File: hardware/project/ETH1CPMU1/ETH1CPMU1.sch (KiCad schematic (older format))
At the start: 0 parts

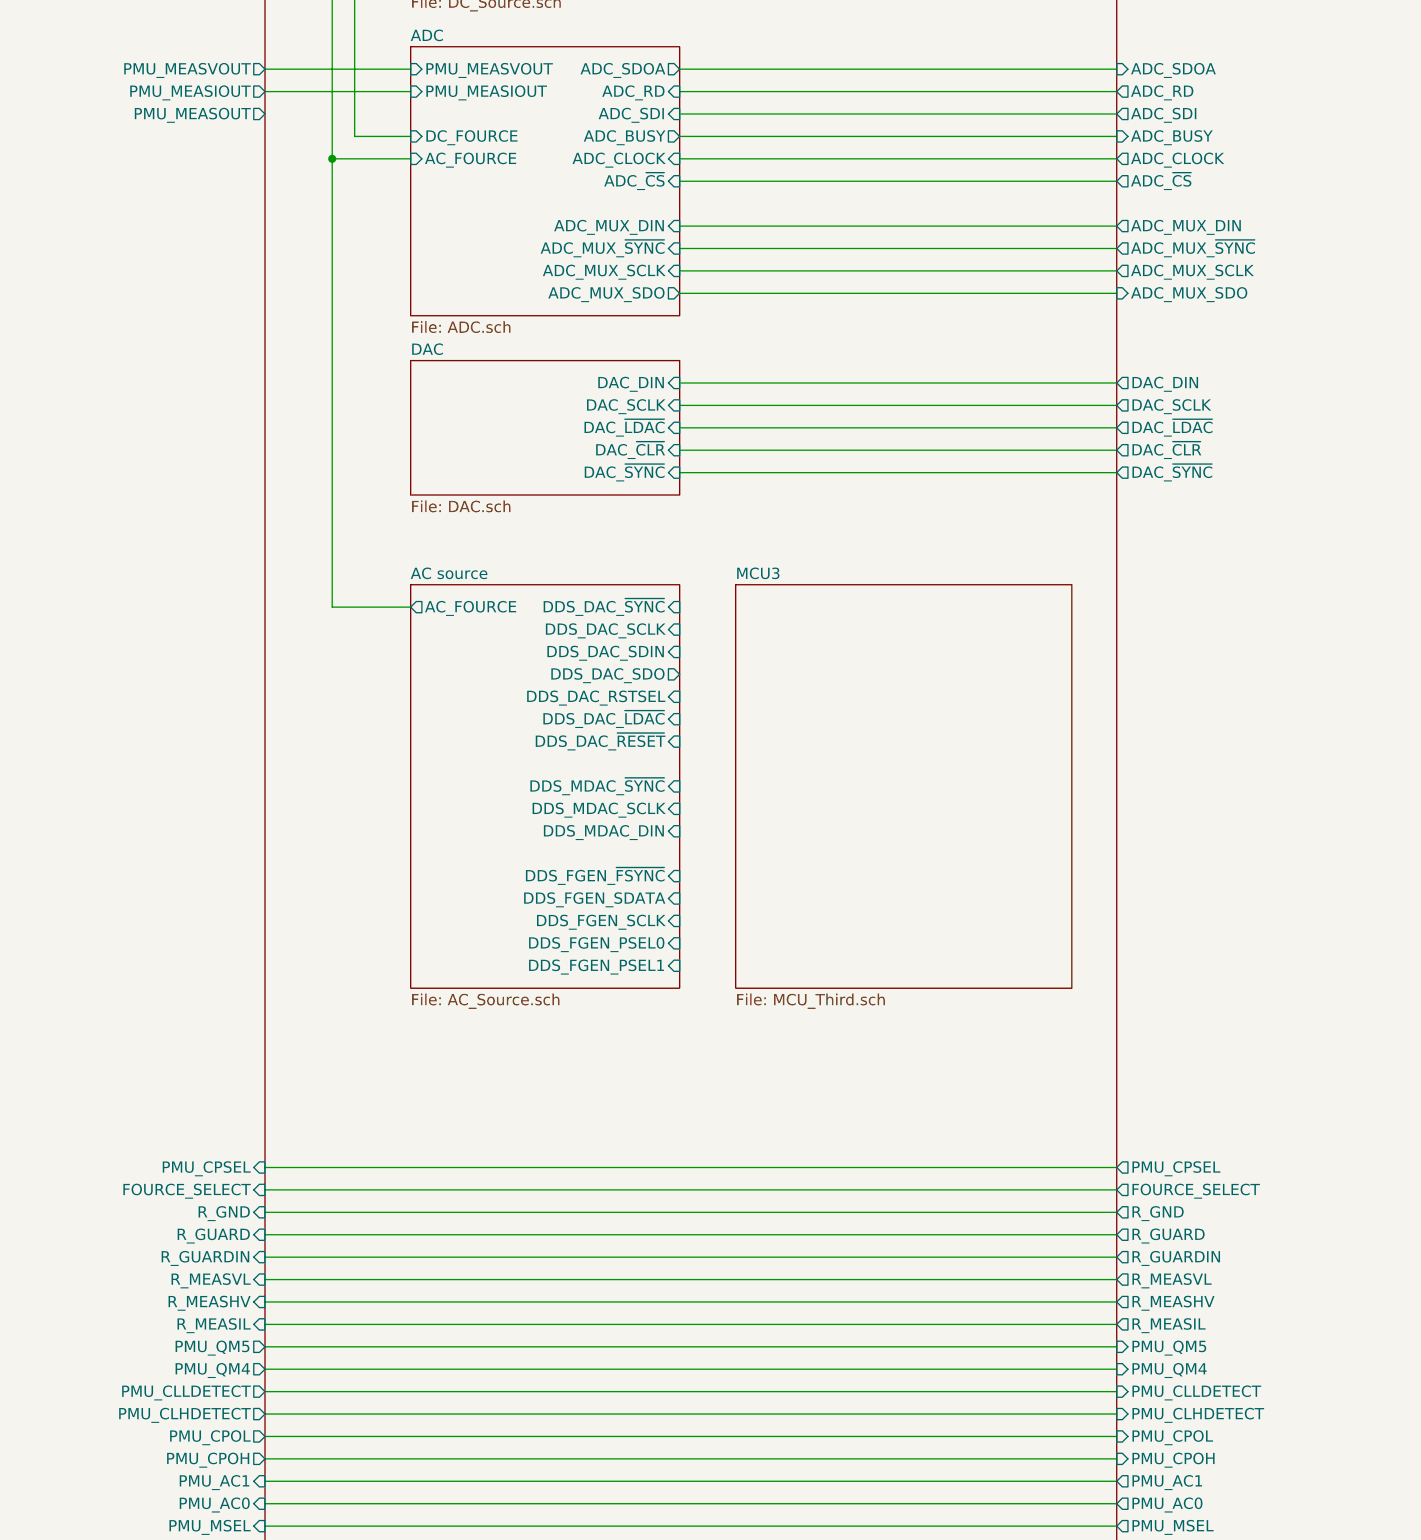
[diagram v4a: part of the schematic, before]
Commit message: New footprint development, changes in schematics.
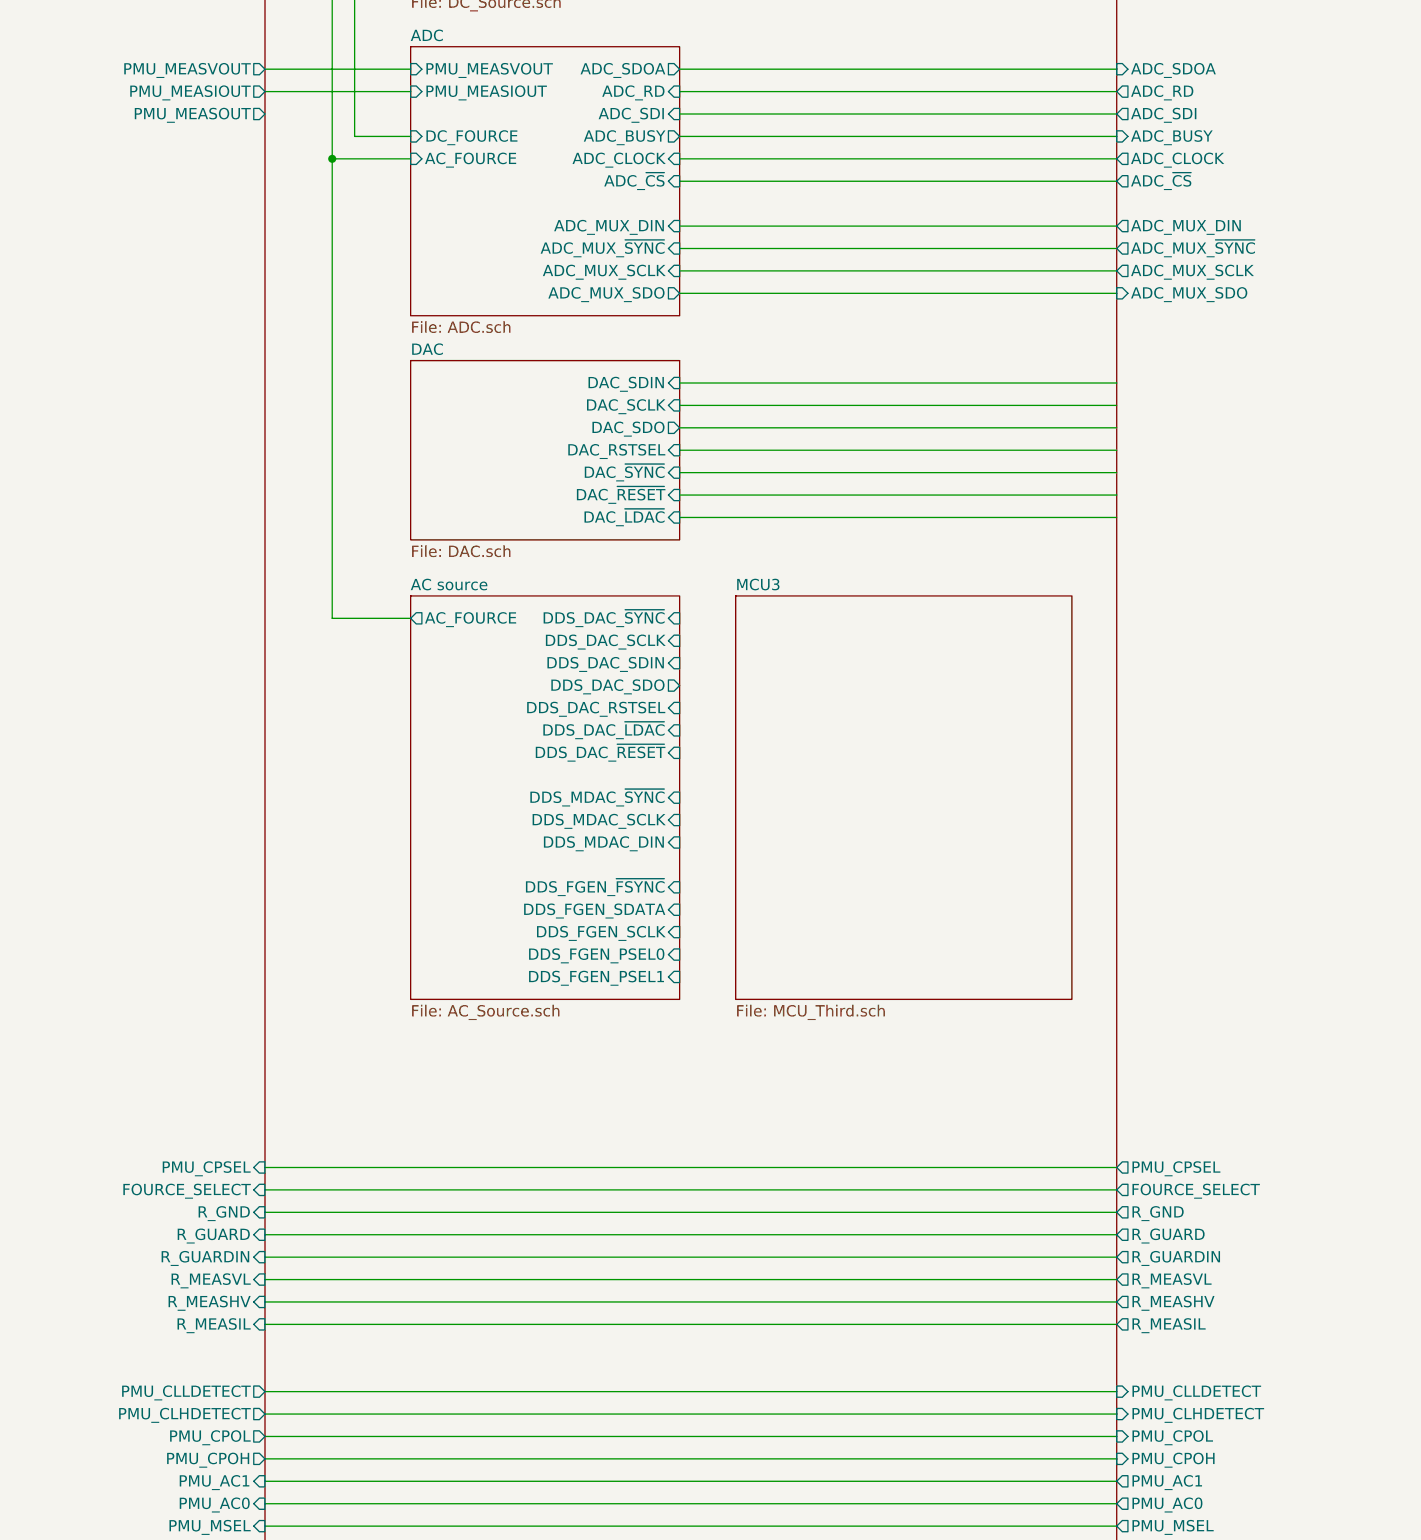
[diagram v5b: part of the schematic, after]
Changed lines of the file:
@@
 $EndSheet
 $Sheet
-S 3750 5200 1200 1800
+S 3750 5250 1200 1800
 U 5DF36C25
 F0 "AC source" 50
 F1 "AC_Source.sch" 50
-F2 "AC_FOURCE" O L 3750 5300 50
-F3 "DDS_DAC_~SYNC" I R 4950 5300 50
-F4 "DDS_DAC_SCLK" I R 4950 5400 50
-F5 "DDS_DAC_SDIN" I R 4950 5500 50
-F6 "DDS_MDAC_~SYNC" I R 4950 6100 50
-F7 "DDS_MDAC_SCLK" I R 4950 6200 50
-F8 "DDS_MDAC_DIN" I R 4950 6300 50
-F9 "DDS_DAC_SDO" O R 4950 5600 50
-F10 "DDS_DAC_~RESET" I R 4950 5900 50
-F11 "DDS_DAC_~LDAC" I R 4950 5800 50
-F12 "DDS_DAC_RSTSEL" I R 4950 5700 50
-F13 "DDS_FGEN_~FSYNC" I R 4950 6500 50
-F14 "DDS_FGEN_SDATA" I R 4950 6600 50
-F15 "DDS_FGEN_SCLK" I R 4950 6700 50
-F16 "DDS_FGEN_PSEL0" I R 4950 6800 50
-F17 "DDS_FGEN_PSEL1" I R 4950 6900 50
-$EndSheet
-$Sheet
-S 3750 4200 1200 600
+F2 "AC_FOURCE" O L 3750 5350 50
+F3 "DDS_DAC_~SYNC" I R 4950 5350 50
+F4 "DDS_DAC_SCLK" I R 4950 5450 50
+F5 "DDS_DAC_SDIN" I R 4950 5550 50
+F6 "DDS_MDAC_~SYNC" I R 4950 6150 50
+F7 "DDS_MDAC_SCLK" I R 4950 6250 50
+F8 "DDS_MDAC_DIN" I R 4950 6350 50
+F9 "DDS_DAC_SDO" O R 4950 5650 50
+F10 "DDS_DAC_~RESET" I R 4950 5950 50
+F11 "DDS_DAC_~LDAC" I R 4950 5850 50
+F12 "DDS_DAC_RSTSEL" I R 4950 5750 50
+F13 "DDS_FGEN_~FSYNC" I R 4950 6550 50
+F14 "DDS_FGEN_SDATA" I R 4950 6650 50
+F15 "DDS_FGEN_SCLK" I R 4950 6750 50
+F16 "DDS_FGEN_PSEL0" I R 4950 6850 50
+F17 "DDS_FGEN_PSEL1" I R 4950 6950 50
+$EndSheet
+$Sheet
+S 3750 4200 1200 800
 U 5DF36C70
 F0 "DAC" 50
 F1 "DAC.sch" 50
-F2 "DAC_DIN" I R 4950 4300 50
+F2 "DAC_~SYNC" I R 4950 4700 50
 F3 "DAC_SCLK" I R 4950 4400 50
-F4 "DAC_~LDAC" I R 4950 4500 50
-F5 "DAC_~CLR" I R 4950 4600 50
-F6 "DAC_~SYNC" I R 4950 4700 50
+F4 "DAC_SDIN" I R 4950 4300 50
+F5 "DAC_SDO" O R 4950 4500 50
+F6 "DAC_~RESET" I R 4950 4800 50
+F7 "DAC_~LDAC" I R 4950 4900 50
+F8 "DAC_RSTSEL" I R 4950 4600 50
 $EndSheet
 Wire Wire Line
@@
 F15 "PMU_CLHDETECT" O R 3100 8900 50
 F16 "PMU_CLLDETECT" O R 3100 8800 50
-F17 "PMU_QM4" O R 3100 8700 50
-F18 "PMU_QM5" O R 3100 8600 50
-F19 "A" B R 3100 1150 50
-F20 "F" B R 3100 1650 50
-F21 "B" B R 3100 1250 50
-F22 "E" B R 3100 1550 50
-F23 "C" B R 3100 1350 50
-F24 "R_MEASIL" I R 3100 8500 50
-F25 "R_MEASHV" I R 3100 8400 50
-F26 "R_MEASVL" I R 3100 8300 50
-F27 "R_GUARDIN" I R 3100 8200 50
-F28 "R_GUARD" I R 3100 8100 50
-F29 "R_GND" I R 3100 8000 50
-F30 "PMU_MEASVOUT" O R 3100 2900 50
-F31 "PMU_MEASIOUT" O R 3100 3000 50
-F32 "DC_FOURCE" I R 3100 1950 50
-F33 "AC_FOURCE" I R 3100 2050 50
-F34 "FOURCE_SELECT" I R 3100 7900 50
-F35 "PMU_CPSEL" I R 3100 7800 50
-F36 "PMU_MEASOUT" O R 3100 3100 50
+F17 "A" B R 3100 1150 50
+F18 "F" B R 3100 1650 50
+F19 "B" B R 3100 1250 50
+F20 "E" B R 3100 1550 50
+F21 "C" B R 3100 1350 50
+F22 "R_MEASIL" I R 3100 8500 50
+F23 "R_MEASHV" I R 3100 8400 50
+F24 "R_MEASVL" I R 3100 8300 50
+F25 "R_GUARDIN" I R 3100 8200 50
+F26 "R_GUARD" I R 3100 8100 50
+F27 "R_GND" I R 3100 8000 50
+F28 "PMU_MEASVOUT" O R 3100 2900 50
+F29 "PMU_MEASIOUT" O R 3100 3000 50
+F30 "DC_FOURCE" I R 3100 1950 50
+F31 "AC_FOURCE" I R 3100 2050 50
+F32 "FOURCE_SELECT" I R 3100 7900 50
+F33 "PMU_CPSEL" I R 3100 7800 50
+F34 "PMU_MEASOUT" O R 3100 3100 50
 $EndSheet
 Wire Wire Line
@@
 Wire Wire Line
 	3100 8800 6900 8800
-Wire Wire Line
-	6900 8700 3100 8700
-Wire Wire Line
-	3100 8600 6900 8600
 Wire Wire Line
 	3750 1950 3500 1950
@@
 F16 "ADC_MUX_SCLK" O L 6900 3800 50
 F17 "ADC_MUX_SDO" I L 6900 3900 50
-F18 "DAC_DIN" O L 6900 4300 50
-F19 "DAC_SCLK" O L 6900 4400 50
-F20 "DAC_~LDAC" O L 6900 4500 50
-F21 "DAC_~CLR" O L 6900 4600 50
-F22 "DAC_~SYNC" O L 6900 4700 50
-F23 "PMU_STANDBY" O L 6900 10200 50
-F24 "PMU_~STB" O L 6900 10100 50
-F25 "PMU_CPCK" O L 6900 10000 50
-F26 "PMU_~MOE" O L 6900 9900 50
-F27 "PMU_~CS" O L 6900 9800 50
-F28 "PMU_AM0" O L 6900 9700 50
-F29 "PMU_AM1" O L 6900 9600 50
-F30 "PMU_AM2" O L 6900 9500 50
-F31 "PMU_CPSEL" O L 6900 7800 50
-F32 "PMU_MSEL" O L 6900 9400 50
-F33 "PMU_AC0" O L 6900 9300 50
-F34 "PMU_AC1" O L 6900 9200 50
-F35 "PMU_CPOH" I L 6900 9100 50
-F36 "PMU_CPOL" I L 6900 9000 50
-F37 "PMU_CLHDETECT" I L 6900 8900 50
-F38 "PMU_CLLDETECT" I L 6900 8800 50
-F39 "PMU_QM4" I L 6900 8700 50
-F40 "PMU_QM5" I L 6900 8600 50
-F41 "R_MEASIL" O L 6900 8500 50
-F42 "R_MEASVL" O L 6900 8300 50
-F43 "R_GUARD" O L 6900 8100 50
-F44 "R_MEASHV" O L 6900 8400 50
-F45 "R_GUARDIN" O L 6900 8200 50
-F46 "R_GND" O L 6900 8000 50
-F47 "FOURCE_SELECT" O L 6900 7900 50
-F48 "MCU2_~SSS" I R 8550 2250 50
-F49 "MCU2_MISO" O R 8550 2150 50
-F50 "MCU2_MOSI" I R 8550 2050 50
-F51 "MCU2_SCLK" I R 8550 1950 50
-F52 "MCU2_GPIO_OUT1" I R 8550 2450 50
-F53 "MCU2_STATUS_IN" O R 8550 2350 50
-F54 "MCU2_GPIO_OUT2" I R 8550 2550 50
+F18 "PMU_STANDBY" O L 6900 10200 50
+F19 "PMU_~STB" O L 6900 10100 50
+F20 "PMU_CPCK" O L 6900 10000 50
+F21 "PMU_~MOE" O L 6900 9900 50
+F22 "PMU_~CS" O L 6900 9800 50
+F23 "PMU_AM0" O L 6900 9700 50
+F24 "PMU_AM1" O L 6900 9600 50
+F25 "PMU_AM2" O L 6900 9500 50
+F26 "PMU_CPSEL" O L 6900 7800 50
+F27 "PMU_MSEL" O L 6900 9400 50
+F28 "PMU_AC0" O L 6900 9300 50
+F29 "PMU_AC1" O L 6900 9200 50
+F30 "PMU_CPOH" I L 6900 9100 50
+F31 "PMU_CPOL" I L 6900 9000 50
+F32 "PMU_CLHDETECT" I L 6900 8900 50
+F33 "PMU_CLLDETECT" I L 6900 8800 50
+F34 "R_MEASIL" O L 6900 8500 50
+F35 "R_MEASVL" O L 6900 8300 50
+F36 "R_GUARD" O L 6900 8100 50
+F37 "R_MEASHV" O L 6900 8400 50
+F38 "R_GUARDIN" O L 6900 8200 50
+F39 "R_GND" O L 6900 8000 50
+F40 "FOURCE_SELECT" O L 6900 7900 50
+F41 "MCU2_~SSS" I R 8550 2250 50
+F42 "MCU2_MISO" O R 8550 2150 50
+F43 "MCU2_MOSI" I R 8550 2050 50
+F44 "MCU2_SCLK" I R 8550 1950 50
+F45 "MCU2_GPIO_OUT1" I R 8550 2450 50
+F46 "MCU2_STATUS_IN" O R 8550 2350 50
+F47 "MCU2_GPIO_OUT2" I R 8550 2550 50
 $EndSheet
 Wire Wire Line
 	6900 7800 3100 7800
 Wire Wire Line
-	3750 5300 3400 5300
-Wire Wire Line
-	3400 5300 3400 3300
+	3750 5350 3400 5350
+Wire Wire Line
+	3400 5350 3400 3300
 Connection ~ 3400 3300
 Wire Wire Line
@@
 	6900 4700 4950 4700
 $Sheet
-S 5200 5200 1500 1800
+S 5200 5250 1500 1800
 U 5E29C232
 F0 "MCU3" 50
@@
 F15 "MCU2_GPIO_OUT2" O L 8750 2550 50
 $EndSheet
+Wire Wire Line
+	4950 4800 6900 4800
+Wire Wire Line
+	4950 4900 6900 4900
 $EndSCHEMATC

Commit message: Schematic design
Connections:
- wire segments 94 -> 120
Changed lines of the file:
@@
 $EndSheet
 $Sheet
-S 3750 5250 1200 1800
+S 3750 5250 1200 2600
 U 5DF36C25
 F0 "AC source" 50
@@
 F7 "DDS_MDAC_SCLK" I R 4950 6250 50
 F8 "DDS_MDAC_DIN" I R 4950 6350 50
-F9 "DDS_DAC_SDO" O R 4950 5650 50
-F10 "DDS_DAC_~RESET" I R 4950 5950 50
-F11 "DDS_DAC_~LDAC" I R 4950 5850 50
-F12 "DDS_DAC_RSTSEL" I R 4950 5750 50
-F13 "DDS_FGEN_~FSYNC" I R 4950 6550 50
-F14 "DDS_FGEN_SDATA" I R 4950 6650 50
-F15 "DDS_FGEN_SCLK" I R 4950 6750 50
-F16 "DDS_FGEN_PSEL0" I R 4950 6850 50
-F17 "DDS_FGEN_PSEL1" I R 4950 6950 50
+F9 "DDS_DAC_~RESET" I R 4950 5850 50
+F10 "DDS_DAC_~LDAC" I R 4950 5750 50
+F11 "DDS_DAC_RSTSEL" I R 4950 5650 50
+F12 "DDS_FGEN_~FSYNC" I R 4950 6550 50
+F13 "DDS_FGEN_SDATA" I R 4950 6650 50
+F14 "DDS_FGEN_PSEL0" I R 4950 6850 50
+F15 "DDS_FGEN_PSEL1" I R 4950 6950 50
+F16 "DDS_FGEN_SCLK" I R 4950 6750 50
+F17 "DDS_MEAS_CLK" I R 4950 7250 50
+F18 "DDS_MEAS_CONV" I R 4950 7350 50
+F19 "DDS_MEAS_DATA" I R 4950 7450 50
+F20 "DDS_MEAS_A0" I R 4950 7550 50
+F21 "DDS_MEAS_A1" I R 4950 7650 50
+F22 "DDS_MEAS_A2" I R 4950 7750 50
+F23 "DDS_DAC_SDO" O R 4950 5950 50
+F24 "DDS_FGEN_FSELECT" I R 4950 7050 50
 $EndSheet
 $Sheet
@@
 F20 "E" B R 3100 1550 50
 F21 "C" B R 3100 1350 50
-F22 "R_MEASIL" I R 3100 8500 50
-F23 "R_MEASHV" I R 3100 8400 50
-F24 "R_MEASVL" I R 3100 8300 50
-F25 "R_GUARDIN" I R 3100 8200 50
-F26 "R_GUARD" I R 3100 8100 50
-F27 "R_GND" I R 3100 8000 50
+F22 "R_MEASIL" I R 3100 8700 50
+F23 "R_MEASHV" I R 3100 8600 50
+F24 "R_MEASVL" I R 3100 8500 50
+F25 "R_GUARDIN" I R 3100 8400 50
+F26 "R_GUARD" I R 3100 8300 50
+F27 "R_GND" I R 3100 8200 50
 F28 "PMU_MEASVOUT" O R 3100 2900 50
 F29 "PMU_MEASIOUT" O R 3100 3000 50
 F30 "DC_FOURCE" I R 3100 1950 50
 F31 "AC_FOURCE" I R 3100 2050 50
-F32 "FOURCE_SELECT" I R 3100 7900 50
-F33 "PMU_CPSEL" I R 3100 7800 50
+F32 "FOURCE_SELECT" I R 3100 8100 50
+F33 "PMU_CPSEL" I R 3100 8000 50
 F34 "PMU_MEASOUT" O R 3100 3100 50
 $EndSheet
@@
 	3100 1150 13350 1150
 Wire Wire Line
+	3100 8700 6900 8700
+Wire Wire Line
+	3100 8600 6900 8600
+Wire Wire Line
 	3100 8500 6900 8500
 Wire Wire Line
@@
 	3100 8200 6900 8200
 Wire Wire Line
+	3750 3000 3100 3000
+Wire Wire Line
+	3100 2900 3750 2900
+Wire Wire Line
 	3100 8100 6900 8100
-Wire Wire Line
-	3100 8000 6900 8000
-Wire Wire Line
-	3750 3000 3100 3000
-Wire Wire Line
-	3100 2900 3750 2900
-Wire Wire Line
-	3100 7900 6900 7900
 Wire Wire Line
 	3750 3200 3500 3200
@@
 F24 "PMU_AM1" O L 6900 9600 50
 F25 "PMU_AM2" O L 6900 9500 50
-F26 "PMU_CPSEL" O L 6900 7800 50
+F26 "PMU_CPSEL" O L 6900 8000 50
 F27 "PMU_MSEL" O L 6900 9400 50
 F28 "PMU_AC0" O L 6900 9300 50
@@
 F32 "PMU_CLHDETECT" I L 6900 8900 50
 F33 "PMU_CLLDETECT" I L 6900 8800 50
-F34 "R_MEASIL" O L 6900 8500 50
-F35 "R_MEASVL" O L 6900 8300 50
-F36 "R_GUARD" O L 6900 8100 50
-F37 "R_MEASHV" O L 6900 8400 50
-F38 "R_GUARDIN" O L 6900 8200 50
-F39 "R_GND" O L 6900 8000 50
-F40 "FOURCE_SELECT" O L 6900 7900 50
+F34 "R_MEASIL" O L 6900 8700 50
+F35 "R_MEASVL" O L 6900 8500 50
+F36 "R_GUARD" O L 6900 8300 50
+F37 "R_MEASHV" O L 6900 8600 50
+F38 "R_GUARDIN" O L 6900 8400 50
+F39 "R_GND" O L 6900 8200 50
+F40 "FOURCE_SELECT" O L 6900 8100 50
 F41 "MCU2_~SSS" I R 8550 2250 50
 F42 "MCU2_MISO" O R 8550 2150 50
@@
 F46 "MCU2_STATUS_IN" O R 8550 2350 50
 F47 "MCU2_GPIO_OUT2" I R 8550 2550 50
-$EndSheet
-Wire Wire Line
-	6900 7800 3100 7800
+F48 "DAC_SDIN" O L 6900 4300 50
+F49 "DAC_SCLK" O L 6900 4400 50
+F50 "DAC_~LDAC" O L 6900 4900 50
+$EndSheet
+Wire Wire Line
+	6900 8000 3100 8000
 Wire Wire Line
 	3750 5350 3400 5350
@@
 	6900 4700 4950 4700
 $Sheet
-S 5200 5250 1500 1800
+S 5200 5250 1450 2600
 U 5E29C232
 F0 "MCU3" 50
 F1 "MCU_Third.sch" 50
+F2 "DDS_FGEN_~FSYNC" O L 5200 6550 50
+F3 "DDS_FGEN_SDATA" O L 5200 6650 50
+F4 "DDS_FGEN_SCLK" O L 5200 6750 50
+F5 "DDS_MDAC_~SYNC" O L 5200 6150 50
+F6 "DDS_MDAC_SCLK" O L 5200 6250 50
+F7 "DDS_MDAC_DIN" O L 5200 6350 50
+F8 "DDS_MEAS_CLK" O L 5200 7250 50
+F9 "DDS_MEAS_CONV" O L 5200 7350 50
+F10 "DDS_MEAS_DATA" O L 5200 7450 50
+F11 "DDS_DAC_~SYNC" O L 5200 5350 50
+F12 "DDS_DAC_SCLK" O L 5200 5450 50
+F13 "DDS_DAC_SDIN" O L 5200 5550 50
+F14 "MCU3_SCLK" I R 6650 5350 50
+F15 "MCU3_MISO" O R 6650 5450 50
+F16 "MCU3_MOSI" I R 6650 5550 50
+F17 "MCU3_NSS" I R 6650 5650 50
+F18 "DDS_DAC_~RESET" O L 5200 5850 50
+F19 "DDS_DAC_~LDAC" O L 5200 5750 50
+F20 "DDS_DAC_RSTSEL" O L 5200 5650 50
+F21 "DDS_MEAS_A0" O L 5200 7550 50
+F22 "DDS_MEAS_A1" O L 5200 7650 50
+F23 "DDS_MEAS_A2" O L 5200 7750 50
+F24 "DDS_DAC_SDO" I L 5200 5950 50
+F25 "DDS_FGEN_PSEL0" O L 5200 6850 50
+F26 "DDS_FGEN_PSEL1" O L 5200 6950 50
+F27 "DDS_FGEN_FSELECT" O L 5200 7050 50
 $EndSheet
 $Sheet
@@
 Wire Wire Line
 	4950 4900 6900 4900
+Wire Wire Line
+	5200 7250 4950 7250
+Wire Wire Line
+	4950 7350 5200 7350
+Wire Wire Line
+	5200 7450 4950 7450
+Wire Wire Line
+	5200 6750 4950 6750
+Wire Wire Line
+	4950 6550 5200 6550
+Wire Wire Line
+	5200 6650 4950 6650
+Wire Wire Line
+	4950 6350 5200 6350
+Wire Wire Line
+	5200 6250 4950 6250
+Wire Wire Line
+	4950 6150 5200 6150
+Wire Wire Line
+	5200 5550 4950 5550
+Wire Wire Line
+	4950 5450 5200 5450
+Wire Wire Line
+	5200 5350 4950 5350
+Wire Wire Line
+	6650 5350 6900 5350
+Wire Wire Line
+	6650 5450 6900 5450
+Wire Wire Line
+	6650 5550 6900 5550
+Wire Wire Line
+	6650 5650 6900 5650
+Wire Wire Line
+	5200 5650 4950 5650
+Wire Wire Line
+	4950 5750 5200 5750
+Wire Wire Line
+	5200 5850 4950 5850
+Wire Wire Line
+	4950 7550 5200 7550
+Wire Wire Line
+	5200 7650 4950 7650
+Wire Wire Line
+	4950 7750 5200 7750
+Wire Wire Line
+	5200 5950 4950 5950
+Wire Wire Line
+	4950 6850 5200 6850
+Wire Wire Line
+	5200 6950 4950 6950
+Wire Wire Line
+	4950 7050 5200 7050
 $EndSCHEMATC

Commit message: Schematic design
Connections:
- wire segments 120 -> 123

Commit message: PCB design.
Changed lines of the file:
@@
 F15 "ADC_MUX_SDO" O R 4950 3900 50
 F16 "PMU_MEASOUT" I L 3750 3100 50
+F17 "ADC_CONVST" I R 4950 3500 50
 $EndSheet
 Wire Wire Line
@@
 F57 "MCU3_MISO" I L 6900 5450 50
 F58 "MCU3_MOSI" O L 6900 5550 50
+F59 "ADC_CONVST" O L 6900 3500 50
 $EndSheet
 Wire Wire Line
@@
 Wire Wire Line
 	3100 4400 3750 4400
+Wire Wire Line
+	6900 3500 4950 3500
 $EndSCHEMATC
